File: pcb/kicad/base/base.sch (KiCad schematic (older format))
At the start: 17 parts, among them P1 CONN_01X02, U1 SAMB11G18A, Y1 26MHz, Y2 32.768kHz

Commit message: Add complete schematic for base central
SWD connection has been completed along with power connections.
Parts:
- added C10, C18: 1.0uF, symbol C_Small
- added C11, C12, C13, C14, C15: 0.1uF, symbol C_Small
- added C16: 2.2uF, symbol C_Small
- added C17: 0.01uF, symbol C_Small
- added C19: C_Small, symbol C_Small
- added FB1: BLM03AG121SN1, symbol Ferrite_Bead_Small
- added L1: 9.1nH, symbol L_Small
- added L2: 4.7uH, symbol L_Small
- added R1: 0, symbol R_Small
- added R2: 10k, symbol R_Small
- added R3: 100k, symbol R_Small
- C1: renamed from C9; value C_Small -> DNI
- C2: renamed from C8; value C_Small -> DNI
- L2: renamed from L1; value 4.3nH -> 3nH
- gave numbers to parts that had none: 1
- renumbered C7 to C3, C6 to C4, C3 to C6, C4 to C7, C1 to C8, C2 to C9, L2 to L1, Y2 to Y1, Y1 to Y2
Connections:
- net labels added: +3.3V, +5V, SIG_2.4G, SWDCLK, SWO
- net labels removed: SWCLK
- wire segments 33 -> 75
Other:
- note added: "Place C10 as close as possible to pin 4.\nPlace C11 as close as possible to pin 48.\nPlace C12 as close as possible to pin 1.\nPlace C13 as close as possible to pin 2."
- moved on the sheet: AE1, C1, C2, C3, C4, C6, C8, L1, L2, P2

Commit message: Add schematic for base transceiver
Finished symbol and footprint for XBee PRO, and connected through
hierarchy to central. Footprints for both crystals still need to be
completed.
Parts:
- added P3: CONN_01X02, symbol CONN_01X02
- renumbered L1 to L3, L2 to L4
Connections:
- net labels added: GPIO_MS1, GPIO_MS2, GPIO_MS3, GPIO_MS4, LP_GPIO_10, LP_GPIO_11, LP_GPIO_12, LP_GPIO_13, LP_GPIO_14, LP_GPIO_15, LP_GPIO_16, LP_GPIO_17, LP_GPIO_18, LP_GPIO_19, LP_GPIO_2, LP_GPIO_20, LP_GPIO_22, LP_GPIO_23, LP_GPIO_3, LP_GPIO_4, LP_GPIO_5, LP_GPIO_6, LP_GPIO_7, LP_GPIO_8, LP_GPIO_9, Wake
- wire segments 75 -> 86
- no-connect marks 5 -> 7
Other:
- note added: "If Wake function is not used,\nconnect AO_GPIO_0 to GND."
- moved on the sheet: AE1, C1, C10, C11, C12, C13, C14, C15, C16, C17, C18, C19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

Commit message: Add initial layout for base daughterboard
Started the initial layout of the daughterboard with the
microcontroller. The inductors and crystals have placeholder footprints,
while the antenna and ferrite bead are TBD. Currently using default SMD
0402 size, but compact layout is still difficult to achieve. Crystals
have been placed as close as possible to the oscillator pins, but ground
return path is not optimized. Extent of components to be placed on
daughterboard still not finalized.
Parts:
- removed Y1: 32.768kHz, symbol Crystal_GND3_Small
- removed Y2: 26MHz, symbol Crystal_GND3_Small
- added P4: Vbatt_I-test, Socket_Strips:Socket_Strip_Straight_1x02_Pitch2.54mm, symbol CONN_01X02
- added P5: CHIP_EN, Socket_Strips:Socket_Strip_Straight_1x02_Pitch2.54mm, symbol CONN_01X02
- added Y1: 32.768kHz, Crystals:Crystal_C38-LF_d3.0mm_l8.0mm_Horizontal, symbol Crystal_Small
- added Y2: 26MHz, Crystals:Crystal_SMD_3225-4pin_3.2x2.5mm_HandSoldering, symbol Crystal_GND24_Small
- C1, C10, C11, C12, C13, C14, C15, C16, C17, C18, C19, C2, C3, C4, C5, C6, C7, C8, C9, L1, L2, L3, L4, R1, R2, R3: footprint (none) -> Capacitors_SMD:C_0402
- P1: value CONN_01X02 -> Test_MUX; footprint (none) -> Socket_Strips:Socket_Strip_Straight_1x02_Pitch2.54mm
- P2: value CONN_02X10 -> J-Link SWD; footprint (none) -> Socket_Strips:Socket_Strip_Straight_2x10_Pitch2.54mm
- P3: value CONN_01X02 -> Vbatt-V_test; footprint (none) -> Socket_Strips:Socket_Strip_Straight_1x02_Pitch2.54mm
- U1: footprint QFN-48-1EP_6x6mm_Pitch0.4mm -> Housings:QFN-48-1EP_6x6mm_Pitch0.4mm
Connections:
- wire segments 86 -> 90
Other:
- moved on the sheet: C6, C7

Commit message: Cleanup crystals and 2.4GHz RF end
UART pins dedicated for 900MHz XBee operations may need to be moved,
keeping the 2.4GHz and 900MHz signals as far apart as possible. SMA jack
substituted for 2.4GHz antenna for first prototype; expecting to measure
input impedance.
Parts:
- removed P1: Test_MUX, Socket_Strips:Socket_Strip_Straight_1x02_Pitch2.54mm, symbol CONN_01X02
- added P2: CONN_01X02, Misc:Molex_SMA_Jack_Edge_Mount, symbol CONN_01X02
- renumbered P2 to P1
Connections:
- wire segments 90 -> 88
- no-connect marks 7 -> 9
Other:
- moved on the sheet: AE1
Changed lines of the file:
@@
 EESchema Schematic File Version 2
-LIBS:rf_transceivers
-LIBS:microcontrollers
 LIBS:power
 LIBS:device
@@
 LIBS:memory
 LIBS:xilinx
+LIBS:microcontrollers
 LIBS:dsp
 LIBS:microchip
@@
 LIBS:contrib
 LIBS:valves
+LIBS:rf_transceivers
 LIBS:base-cache
 EELAYER 25 0
@@
 L Antenna AE1
 U 1 1 58BAE3A5
-P 2175 2850
-F 0 "AE1" H 2100 2925 50  0000 R CNN
-F 1 "2.4-2.4835GHz" H 2100 2850 50  0000 R CNN
-F 2 "" H 2175 2850 50  0001 C CNN
-F 3 "" H 2175 2850 50  0001 C CNN
-	1    2175 2850
+P 1675 2850
+F 0 "AE1" H 1600 2925 50  0000 R CNN
+F 1 "2.4-2.4835GHz" H 1600 2850 50  0000 R CNN
+F 2 "" H 1675 2850 50  0001 C CNN
+F 3 "" H 1675 2850 50  0001 C CNN
+	1    1675 2850
 	1    0    0    -1
 $EndComp
@@
 	1    4550 3350
 	1    0    0    -1
-$EndComp
-$Comp
-L CONN_01X02 P1
-U 1 1 58BB3608
-P 5350 4800
-F 0 "P1" V 5350 4975 50  0000 C CNN
-F 1 "Test_MUX" V 5450 4800 50  0000 C CNN
-F 2 "Socket_Strips:Socket_Strip_Straight_1x02_Pitch2.54mm" H 5350 4800 50  0001 C CNN
-F 3 "" H 5350 4800 50  0000 C CNN
-	1    5350 4800
-	0    -1   1    0
 $EndComp
 NoConn ~ 8175 4800
@@
 	5650 4600 5850 4600
 Wire Wire Line
-	5300 4600 5325 4600
-Wire Wire Line
-	5400 4600 5375 4600
-Wire Wire Line
 	8175 4900 8175 5700
 Connection ~ 8175 5000
@@
 SIG_2.4G
 $Comp
-L CONN_02X10 P2
+L CONN_02X10 P1
 U 1 1 58BBB586
 P 7925 5250
-F 0 "P2" H 7925 5800 50  0000 C CNN
+F 0 "P1" H 7925 5800 50  0000 C CNN
 F 1 "J-Link SWD" V 7925 5250 50  0000 C CNN
 F 2 "Socket_Strips:Socket_Strip_Straight_2x10_Pitch2.54mm" H 7925 4050 50  0001 C CNN
@@
 Wire Wire Line
 	4350 3850 4350 4000
+$Comp
+L CONN_01X02 P2
+U 1 1 58BE1BD4
+P 1975 3100
+F 0 "P2" H 1975 3250 50  0000 C CNN
+F 1 "CONN_01X02" V 2075 3100 50  0000 C CNN
+F 2 "Misc:Molex_SMA_Jack_Edge_Mount" H 1975 3100 50  0001 C CNN
+F 3 "" H 1975 3100 50  0000 C CNN
+	1    1975 3100
+	-1   0    0    -1
+$EndComp
+$Comp
+L GND #PWR023
+U 1 1 58BE519F
+P 2175 3150
+F 0 "#PWR023" H 2175 2900 50  0001 C CNN
+F 1 "GND" H 2175 3025 50  0000 C CNN
+F 2 "" H 2175 3150 50  0000 C CNN
+F 3 "" H 2175 3150 50  0000 C CNN
+	1    2175 3150
+	1    0    0    -1
+$EndComp
+NoConn ~ 5325 4600
+NoConn ~ 5375 4600
 $EndSCHEMATC

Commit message: Add more progress to crystal and XBee routing
Crystal has been moved to create a cleaner top layer for better signal
pathing. Daughterboard concept starting to be realized by adding vias
of pin header dimensions. Power routing still needs to be redone, and
and holes for ground header pins need to be placed.
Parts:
- FB1: footprint (none) -> Capacitors_SMD:C_0603_HandSoldering
- P3: value Vbatt-V_test -> Power Source
- renumbered P5 to J1, P4 to J2
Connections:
- net labels added: UART_CTS, UART_RTS, UART_RX, UART_TX
- net labels removed: GPIO_MS1, GPIO_MS2, GPIO_MS3, GPIO_MS4, LP_GPIO_14, LP_GPIO_15, LP_GPIO_16, LP_GPIO_17
- wire segments 88 -> 86
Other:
- moved on the sheet: J2, P3

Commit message: Add header pins into design
Header pins have been implemented into design, keeping in mind the
prototyping goal of a daugther-mother board design. For first revision,
the plan has changed to become a single board. For further revisions,
assuming the daugtherboard portion works properly, it will be sheared
and mounted on header pins, positioned meticulously with convenient
vias. Power is almost completely routed. Ground vias to be completed.
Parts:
- removed U1: SAMB11G18A, Housings:QFN-48-1EP_6x6mm_Pitch0.4mm, symbol SAMB11G18A
- added P4: CONN_01X08, Misc:Socket_Strip_Straight_1x08_Pitch2.54mm_Drill0.64mm, symbol CONN_01X08
- added U1: SAMB11G18A-edit, QFN-48-1EP_6x6mm_Pitch0.4mm, symbol SAMB11G18A-edit
- C14: value 0.1uF -> 4.7uF 6.3V
- C16: value 2.2uF -> 2.2uF 6.3V
- J1, J2, P3: footprint Socket_Strips:Socket_Strip_Straight_1x02_Pitch2.54mm -> Misc:Socket_Strip_Straight_1x02_Pitch2.54mm_Drill0.64mm
- L4: footprint Capacitors_SMD:C_0402 -> Capacitors_SMD:C_0805_HandSoldering
- P1: footprint Socket_Strips:Socket_Strip_Straight_2x10_Pitch2.54mm -> Misc:Socket_Strip_Straight_2x10_Pitch2.54mm_Drill0.64mm
- P2: value CONN_01X02 -> SMA
- Y1: footprint Crystals:Crystal_C38-LF_d3.0mm_l8.0mm_Horizontal -> Crystals:Crystal_C38-LF_d3.0mm_l8.0mm_Horizontal_1EP_style1
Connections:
- wire segments 86 -> 123
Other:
- moved on the sheet: FB1, J2, P3, R1

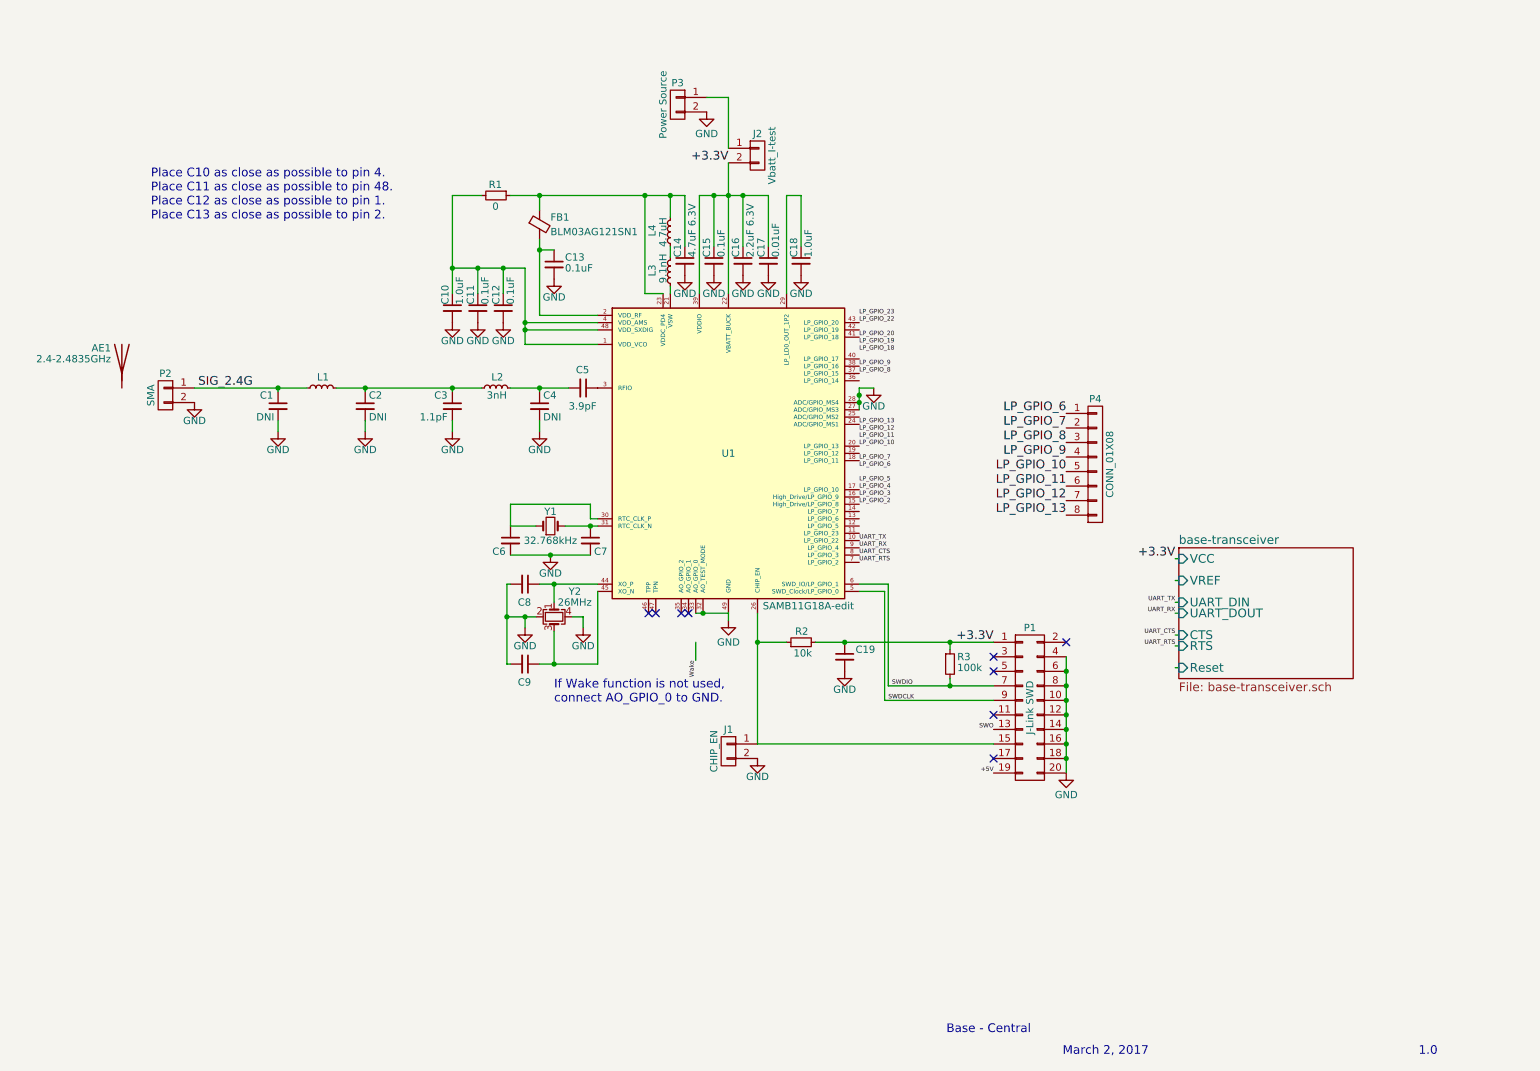
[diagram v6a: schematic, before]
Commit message: Cleanup base schematic and layout
Power routes have been placed to completely cover the entire board.
Crystal adjusted slightly to avoid the UART TX signal line. More vias
dispersed around the board for better ground connections. Gerber files
have been created and are ready to be tiled.
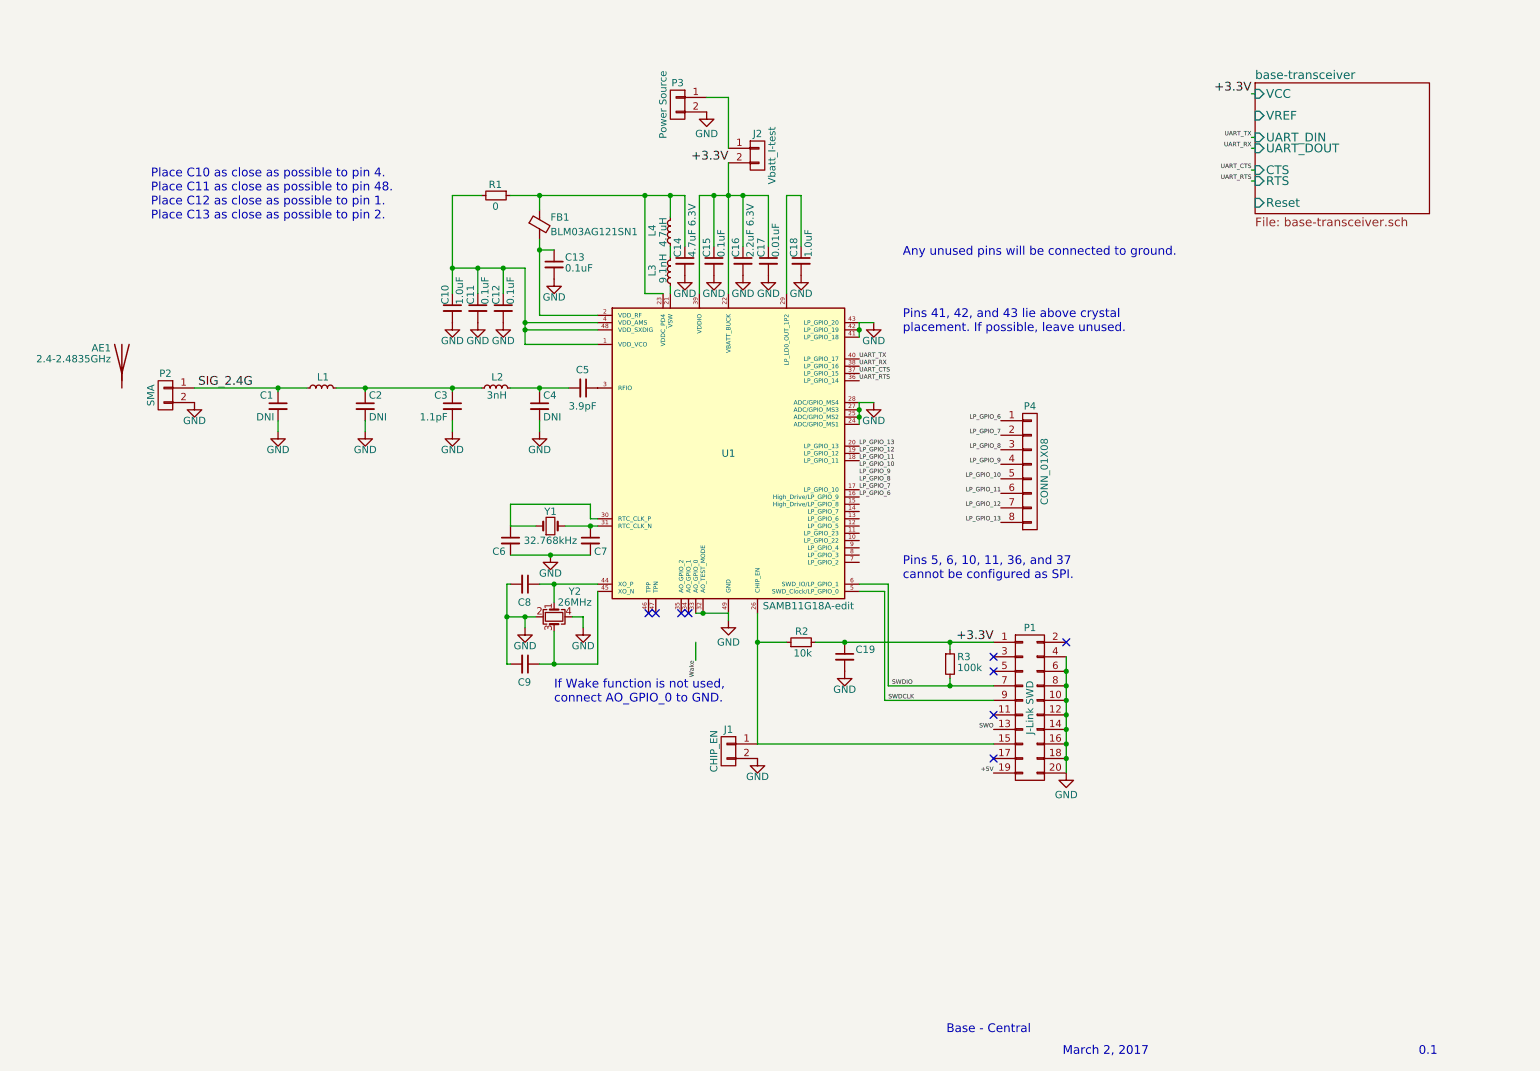
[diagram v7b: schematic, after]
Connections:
- net LP_GPIO_20 is gone; now on net GND: U1.41 (LP_GPIO_18)
- net LP_GPIO_22 is gone; now on net GND: U1.43 (LP_GPIO_20)
- net LP_GPIO_3 is gone; now on net LP_GPIO_6: U1.16 (High_Drive/LP_GPIO_9)
- net LP_GPIO_4 is gone; now on net LP_GPIO_7: U1.17 (LP_GPIO_10)
- net GND: now also U1.24 (ADC/GPIO_MS1), U1.25 (ADC/GPIO_MS2), U1.42 (LP_GPIO_19)
- net LP_GPIO_10: no longer U1.20 (LP_GPIO_13)
- net LP_GPIO_11: now also U1.18 (LP_GPIO_11)
- net LP_GPIO_12: now also U1.19 (LP_GPIO_12)
- net LP_GPIO_13: now also U1.20 (LP_GPIO_13); no longer U1.24 (ADC/GPIO_MS1)
- net LP_GPIO_7: no longer U1.18 (LP_GPIO_11)
- net LP_GPIO_8: no longer U1.37 (LP_GPIO_15)
- net LP_GPIO_9: no longer U1.38 (LP_GPIO_16)
- net UART_CTS: now also U1.37 (LP_GPIO_15); no longer U1.8 (LP_GPIO_3)
- net UART_RTS: now also U1.36 (LP_GPIO_14); no longer U1.7 (LP_GPIO_2)
- net UART_RX: now also U1.38 (LP_GPIO_16); no longer U1.9 (LP_GPIO_4)
- net UART_TX: now also U1.40 (LP_GPIO_17); no longer U1.10 (LP_GPIO_22)
- net LP_GPIO_2: no longer names the net of U1.15 (High_Drive/LP_GPIO_8)
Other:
- note added: "0.1"
- note added: "Any unused pins will be connected to ground."
- note added: "Pins 41, 42, and 43 lie above crystal\nplacement. If possible, leave unused."
- note added: "Pins 5, 6, 10, 11, 36, and 37\ncannot be configured as SPI.\n"
- note removed: "1.0"
- moved on the sheet: P4
